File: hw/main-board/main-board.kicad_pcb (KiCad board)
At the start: 2 copper layers, 42 x 42 mm, 26 parts, among them J1 USB_C_Receptacle_USB2.0_16P, Q1 AONR21307, U1 HUSB238_xxxDD, U2 AP63205WU, U3 AP2112K-3.3, U4 PTR54L, U5 TMC2226-SA

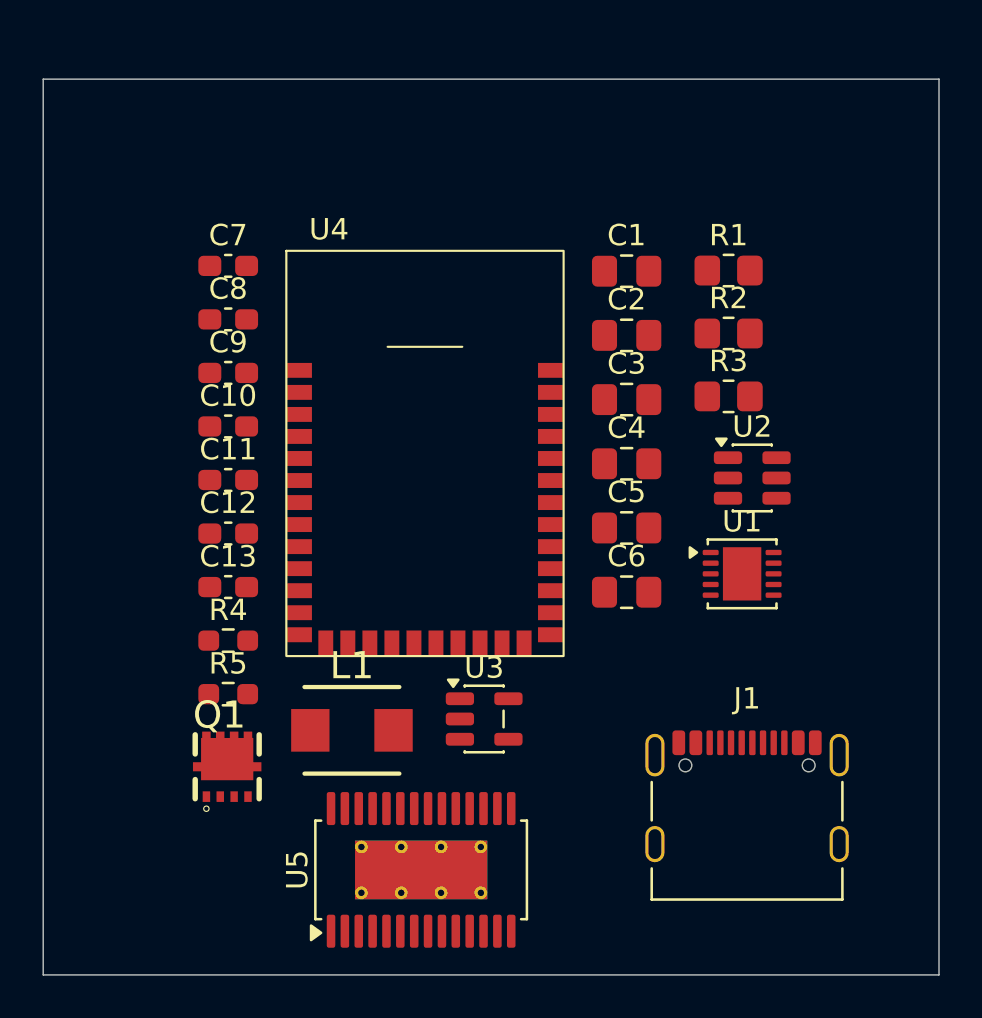
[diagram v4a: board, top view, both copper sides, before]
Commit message: Add TMC2226 circuit
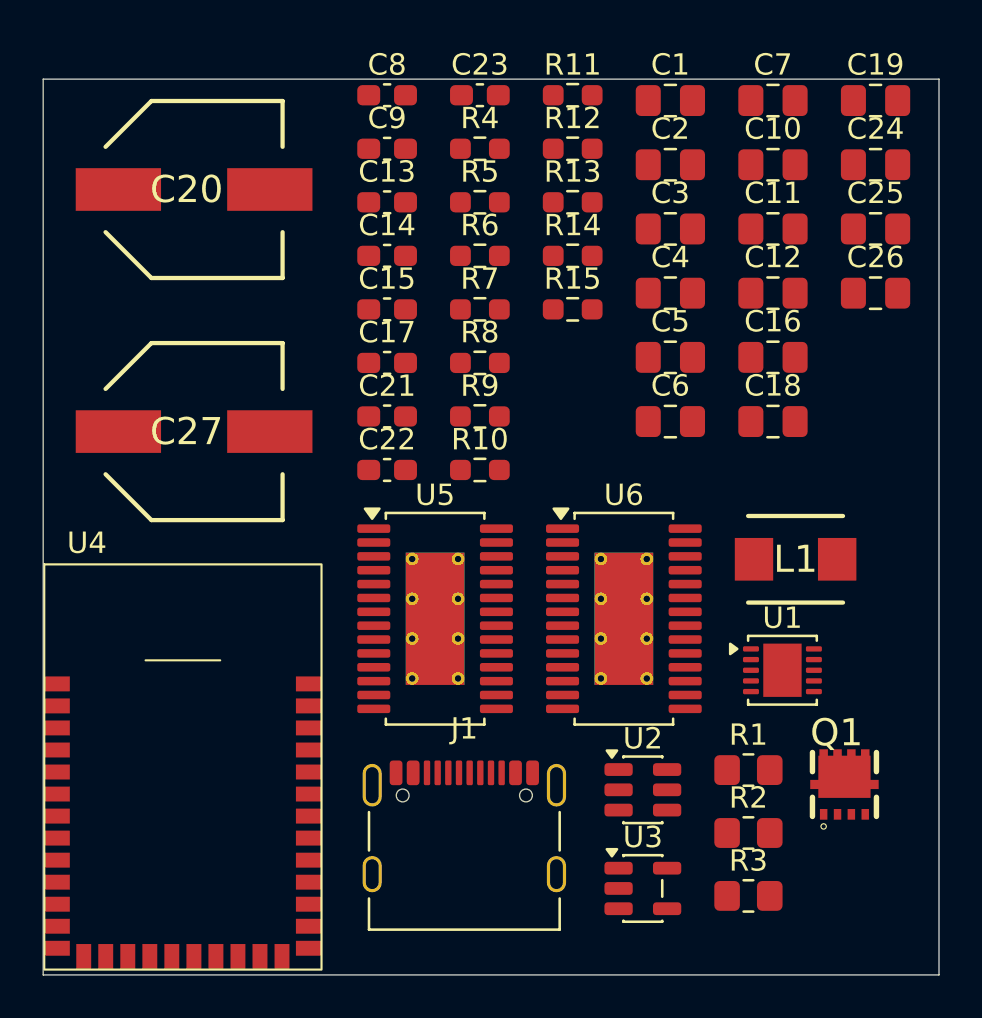
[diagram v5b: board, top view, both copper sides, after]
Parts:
- added C14: 22nF X7R 50V, Capacitor_SMD:C_0603_1608Metric_Pad1.08x0.95mm_HandSolder, F.Cu at (140.6, 81.8)
- added C15: 0.1uF X7R 16V, Capacitor_SMD:C_0603_1608Metric_Pad1.08x0.95mm_HandSolder, F.Cu at (140.6, 84.3)
- added C16: 4.7uF, Capacitor_SMD:C_0805_2012Metric_Pad1.18x1.45mm_HandSolder, F.Cu at (158.7, 86.5)
- added C17: 0.1uF X7R 16V, Capacitor_SMD:C_0603_1608Metric_Pad1.08x0.95mm_HandSolder, F.Cu at (140.6, 86.8)
- added C18: 0.1uF, Capacitor_SMD:C_0805_2012Metric_Pad1.18x1.45mm_HandSolder, F.Cu at (158.7, 89.6)
- added C19: 0.1uF, Capacitor_SMD:C_0805_2012Metric_Pad1.18x1.45mm_HandSolder, F.Cu at (163.5, 74.5)
- added C20: EEE-FK1V101P, Samacsys:EEHZT1E331UP, F.Cu at (131.6, 78.7)
- added C21: 0.1uF X7R 16V, Capacitor_SMD:C_0603_1608Metric_Pad1.08x0.95mm_HandSolder, F.Cu at (140.6, 89.3)
- added C22: 0.1uF X7R 16V, Capacitor_SMD:C_0603_1608Metric_Pad1.08x0.95mm_HandSolder, F.Cu at (140.6, 91.8)
- added C23: 22nF X7R 50V, Capacitor_SMD:C_0603_1608Metric_Pad1.08x0.95mm_HandSolder, F.Cu at (145.0, 74.3)
- added C24: 4.7uF, Capacitor_SMD:C_0805_2012Metric_Pad1.18x1.45mm_HandSolder, F.Cu at (163.5, 77.5)
- added C25: 0.1uF, Capacitor_SMD:C_0805_2012Metric_Pad1.18x1.45mm_HandSolder, F.Cu at (163.5, 80.5)
- added C26: 0.1uF, Capacitor_SMD:C_0805_2012Metric_Pad1.18x1.45mm_HandSolder, F.Cu at (163.5, 83.5)
- added C27: EEE-FK1V101P, Samacsys:EEHZT1E331UP, F.Cu at (131.6, 90.0)
- added R10: 8K2, Resistor_SMD:R_0603_1608Metric_Pad0.98x0.95mm_HandSolder, F.Cu at (145.0, 91.8)
- added R11: 1K, Resistor_SMD:R_0603_1608Metric_Pad0.98x0.95mm_HandSolder, F.Cu at (149.3, 74.3)
- added R12: 10K, Resistor_SMD:R_0603_1608Metric_Pad0.98x0.95mm_HandSolder, F.Cu at (149.3, 76.8)
- added R13: 10K, Resistor_SMD:R_0603_1608Metric_Pad0.98x0.95mm_HandSolder, F.Cu at (149.3, 79.3)
- added R14: 10K, Resistor_SMD:R_0603_1608Metric_Pad0.98x0.95mm_HandSolder, F.Cu at (149.3, 81.8)
- added R15: 8K2, Resistor_SMD:R_0603_1608Metric_Pad0.98x0.95mm_HandSolder, F.Cu at (149.3, 84.3)
- added R6: 10K, Resistor_SMD:R_0603_1608Metric_Pad0.98x0.95mm_HandSolder, F.Cu at (145.0, 81.8)
- added R7: 10K, Resistor_SMD:R_0603_1608Metric_Pad0.98x0.95mm_HandSolder, F.Cu at (145.0, 84.3)
- added R8: 1K, Resistor_SMD:R_0603_1608Metric_Pad0.98x0.95mm_HandSolder, F.Cu at (145.0, 86.8)
- added R9: 10K, Resistor_SMD:R_0603_1608Metric_Pad0.98x0.95mm_HandSolder, F.Cu at (145.0, 89.3)
- added U6: TMC2226-SA, Package_SO:HTSSOP-28-1EP_4.4x9.7mm_P0.65mm_EP2.75x6.2mm_ThermalVias, F.Cu at (151.7, 98.8)
- C10, C11, C12, C7: footprint Capacitor_SMD:C_0603_1608Metric_Pad1.08x0.95mm_HandSolder -> Capacitor_SMD:C_0805_2012Metric_Pad1.18x1.45mm_HandSolder
- moved Q1 29.0 mm to (162.1, 106.6)
- moved C10 28.3 mm to (158.7, 77.5)
- moved C11 28.1 mm to (158.7, 80.5)
- moved C12 27.9 mm to (158.7, 83.5)
- moved C7 26.7 mm to (158.7, 74.5)
- moved R4 25.9 mm to (145.0, 76.8)
- moved R5 25.9 mm to (145.0, 79.3)
- moved R1 23.4 mm to (157.6, 105.9)
- moved R2 23.4 mm to (157.6, 108.8)
- moved R3 23.4 mm to (157.6, 111.8)
- moved L1 22.3 mm to (159.8, 96.0)
- moved C13 19.5 mm to (140.6, 79.3)
- moved U4 18.6 mm to (131.1, 105.8)
- moved U2 15.5 mm to (152.6, 106.8)
- moved J1 13.3 mm to (144.2, 108.5)
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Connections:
- U5 pad 11: unconnected-(U5-5VOUT-Pad11) -> /VREF
- U5 pad 12: unconnected-(U5-MS1_AD0-Pad12) -> Net-(U5-MS1_AD0)
- U5 pad 14: unconnected-(U5-MS2_AD1-Pad14) -> Net-(U5-MS2_AD1)
- U5 pad 15: unconnected-(U5-DIAG-Pad15) -> /DIAG1
- U5 pad 17: unconnected-(U5-CLK-Pad17) -> GND
- U5 pad 18: unconnected-(U5-PDN_UART-Pad18) -> /UART_RX
- U5 pad 19: unconnected-(U5-VCC_IO-Pad19) -> +3.3V
- U5 pad 2: unconnected-(U5-BRB-Pad2) -> GND
- U5 pad 20: unconnected-(U5-STEP-Pad20) -> /STEP1
- U5 pad 21: unconnected-(U5-VREF-Pad21) -> Net-(U5-VREF)
- U5 pad 22: Net-(U5-GND-Pad22) -> GND
- U5 pad 23: unconnected-(U5-DIR-Pad23) -> /DIR1
- U5 pad 26: unconnected-(U5-VS-Pad26) -> VBUS
- U5 pad 27: unconnected-(U5-BRA-Pad27) -> GND
- U5 pad 29: Net-(U5-GND-Pad22) -> GND
- U5 pad 3: unconnected-(U5-VS-Pad3) -> VBUS
- U5 pad 5: unconnected-(U5-~{EN}-Pad5) -> /EN1
- U5 pad 6: Net-(U5-GND-Pad22) -> GND
- U5 pad 7: unconnected-(U5-CPO-Pad7) -> Net-(U5-CPO)
- U5 pad 8: unconnected-(U5-CPI-Pad8) -> Net-(U5-CPI)
- U5 pad 9: unconnected-(U5-VCP-Pad9) -> Net-(U5-VCP)

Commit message: Add connector for motor anf filtering caps for motor coils
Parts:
- added C28: 470pF X7R 100V, Capacitor_SMD:C_0805_2012Metric_Pad1.18x1.45mm_HandSolder, F.Cu at (163.5, 86.5)
- added C29: 470pF X7R 100V, Capacitor_SMD:C_0805_2012Metric_Pad1.18x1.45mm_HandSolder, F.Cu at (163.5, 89.6)
- added C30: 470pF X7R 100V, Capacitor_SMD:C_0805_2012Metric_Pad1.18x1.45mm_HandSolder, F.Cu at (168.3, 74.5)
- added C31: 470pF X7R 100V, Capacitor_SMD:C_0805_2012Metric_Pad1.18x1.45mm_HandSolder, F.Cu at (168.3, 77.5)
- added C32: 470pF X7R 100V, Capacitor_SMD:C_0805_2012Metric_Pad1.18x1.45mm_HandSolder, F.Cu at (168.3, 80.5)
- added C33: 470pF X7R 100V, Capacitor_SMD:C_0805_2012Metric_Pad1.18x1.45mm_HandSolder, F.Cu at (168.3, 83.5)
- added C34: 470pF X7R 100V, Capacitor_SMD:C_0805_2012Metric_Pad1.18x1.45mm_HandSolder, F.Cu at (168.3, 86.5)
- added C35: 470pF X7R 100V, Capacitor_SMD:C_0805_2012Metric_Pad1.18x1.45mm_HandSolder, F.Cu at (168.3, 89.6)
- added J2: 22-23-2041, Samacsys:SHDR4W87P0X254_1X4_1001X635X1105P, F.Cu at (140.4, 97.0)
- added J3: 22-23-2041, Samacsys:SHDR4W87P0X254_1X4_1001X635X1105P, F.Cu at (140.4, 104.9)
- moved L1 21.3 mm to (165.2, 116.6)
- moved U1 19.6 mm to (146.2, 115.9)
- moved Q1 17.3 mm to (145.3, 111.0)
- moved R1 17.3 mm to (140.8, 110.4)
- moved R2 17.3 mm to (140.8, 113.3)
- moved R3 17.3 mm to (140.8, 116.3)
- moved J1 11.6 mm to (155.8, 108.5)
- moved U2 11.6 mm to (164.2, 106.8)
- moved U3 11.6 mm to (164.2, 111.4)
- moved U5 11.6 mm to (154.4, 98.8)
- moved U6 11.6 mm to (163.3, 98.8)
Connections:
- U5 pad 1: unconnected-(U5-OB1-Pad1) -> Net-(U5-OB1)
- U5 pad 25: unconnected-(U5-OA2-Pad25) -> Net-(U5-OA2)
- U5 pad 28: unconnected-(U5-OA1-Pad28) -> Net-(U5-OA1)
- U5 pad 4: unconnected-(U5-OB2-Pad4) -> Net-(U5-OB2)
- U6 pad 1: unconnected-(U6-OB1-Pad1) -> Net-(U6-OB1)
- U6 pad 25: unconnected-(U6-OA2-Pad25) -> Net-(U6-OA2)
- U6 pad 28: unconnected-(U6-OA1-Pad28) -> Net-(U6-OA1)
- U6 pad 4: unconnected-(U6-OB2-Pad4) -> Net-(U6-OB2)

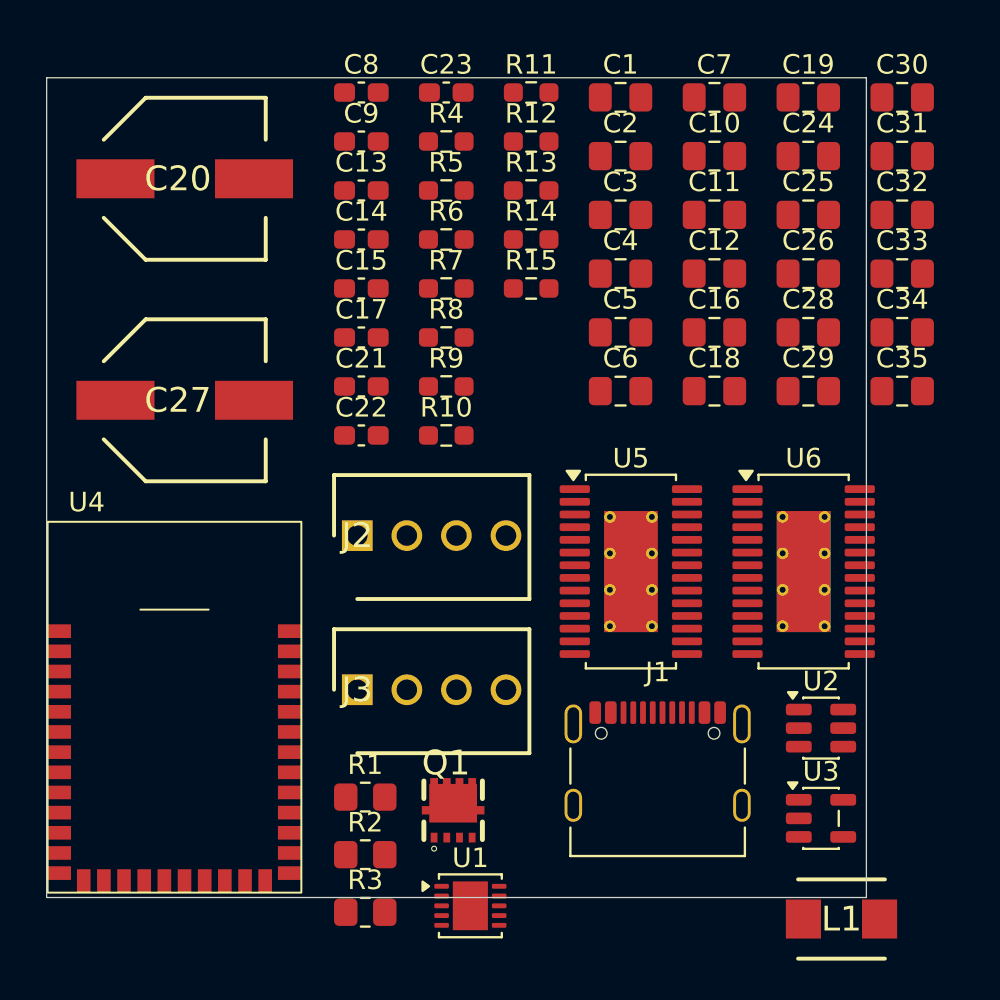
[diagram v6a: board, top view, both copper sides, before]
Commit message: Connector for motor changed, filtering cap changed
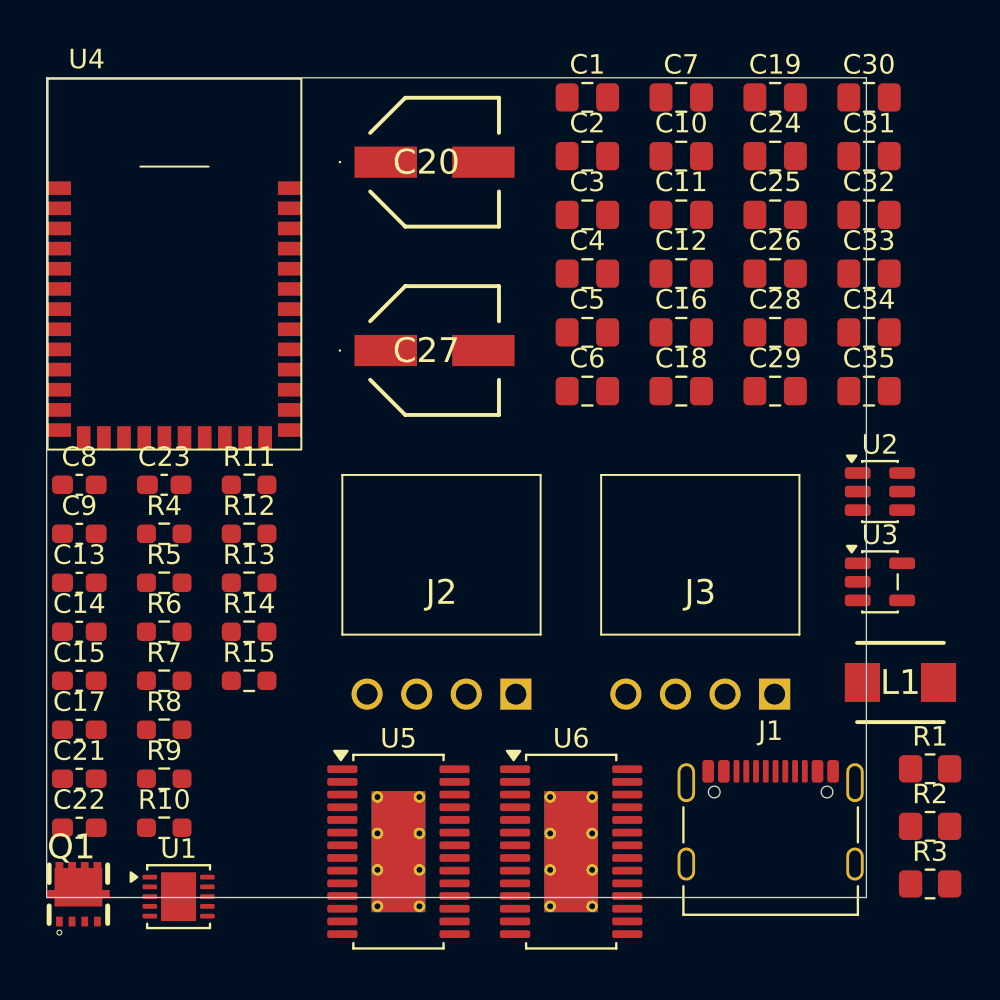
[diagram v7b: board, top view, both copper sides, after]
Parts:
- C20, C27: value EEE-FK1V101P -> EEE-FT1V101AP; footprint Samacsys:EEHZT1E331UP -> Samacsys:EEE1AA101SP
- J2, J3: value 22-23-2041 -> 22-05-3041; footprint Samacsys:SHDR4W87P0X254_1X4_1001X635X1105P -> Samacsys:22053041
- moved R1 29.0 mm to (169.8, 108.9)
- moved R2 29.0 mm to (169.8, 111.9)
- moved R3 29.0 mm to (169.8, 114.8)
- moved C14 24.8 mm to (126.2, 101.9)
- moved C21 24.8 mm to (126.2, 109.4)
- moved C8 24.8 mm to (126.2, 94.4)
- moved C13 24.8 mm to (126.2, 99.4)
- moved C15 24.8 mm to (126.2, 104.4)
- moved C17 24.8 mm to (126.2, 106.9)
- moved C22 24.8 mm to (126.2, 111.9)
- moved C23 24.8 mm to (130.5, 94.4)
- moved C9 24.8 mm to (126.2, 96.9)
- moved R11 24.8 mm to (134.9, 94.4)
- moved R14 24.8 mm to (134.9, 101.9)
- moved R6 24.8 mm to (130.5, 101.9)
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
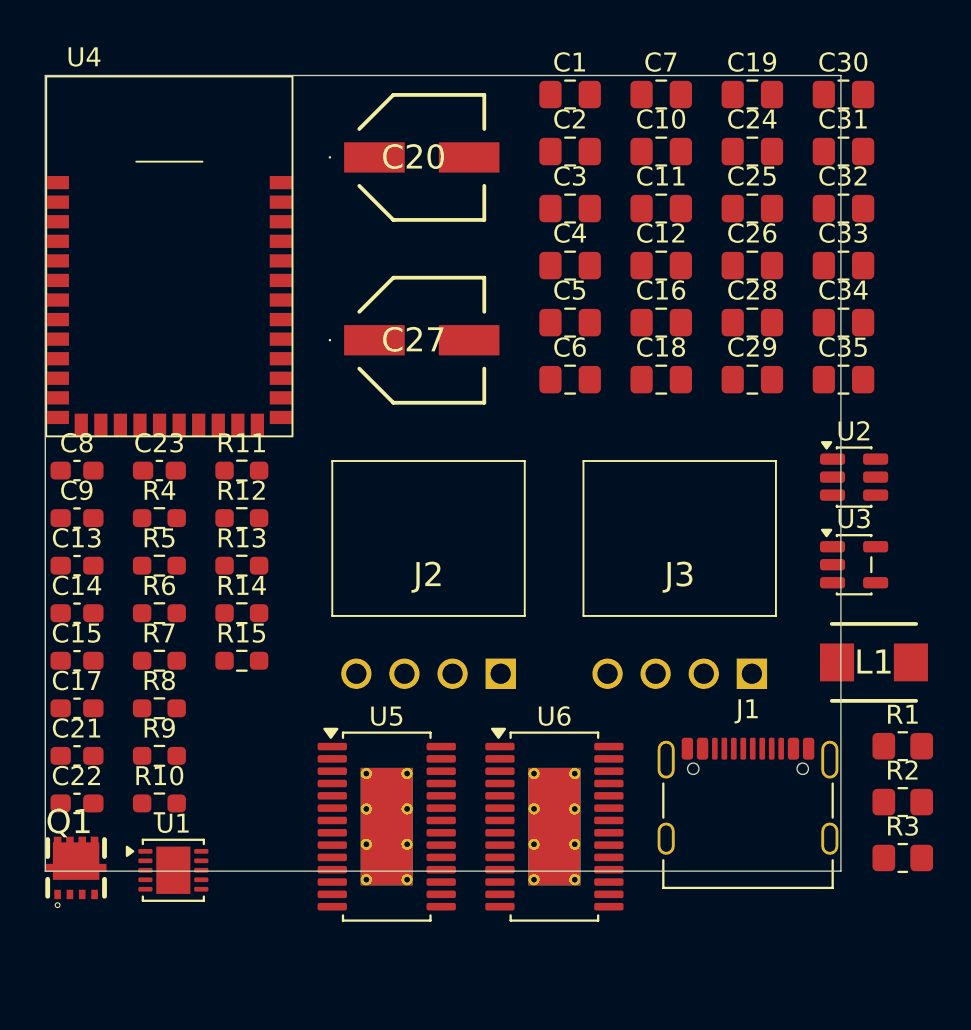
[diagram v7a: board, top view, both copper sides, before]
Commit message: Change connector for motor to smaller one
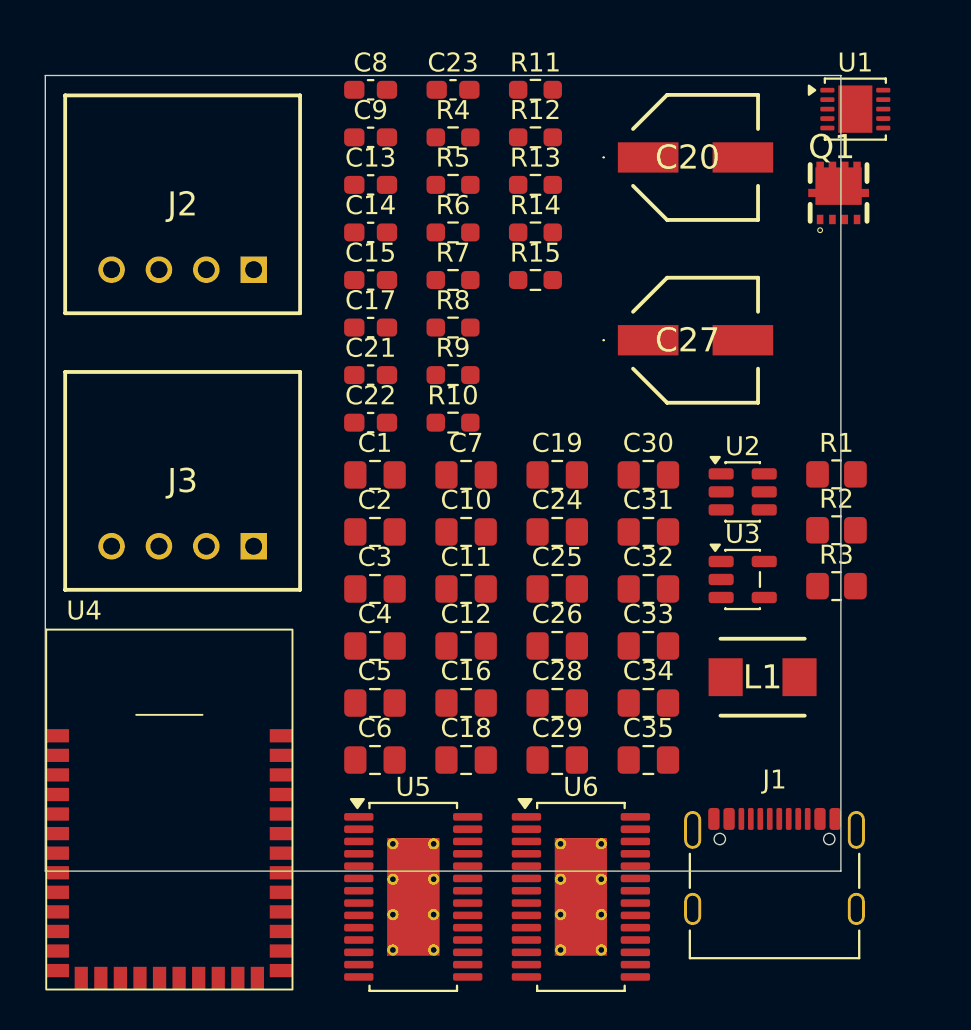
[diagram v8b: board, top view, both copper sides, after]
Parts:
- J2, J3: value 22-05-3041 -> S4B-XH-A_LF__SN_; footprint Samacsys:22053041 -> Samacsys:S4BXHALFSN
- moved U1 53.9 mm to (167.3, 75.3)
- moved Q1 53.8 mm to (166.4, 79.7)
- moved U4 29.2 mm to (131.1, 112.2)
- moved J3 27.1 mm to (135.5, 98.3)
- moved C14 25.4 mm to (141.7, 81.8)
- moved C21 25.4 mm to (141.7, 89.3)
- moved C8 25.4 mm to (141.7, 74.3)
- moved C23 25.4 mm to (146.0, 74.3)
- moved R11 25.4 mm to (150.4, 74.3)
- moved R14 25.4 mm to (150.4, 81.8)
- moved R6 25.4 mm to (146.0, 81.8)
- moved R9 25.4 mm to (146.0, 89.3)
- moved C13 25.4 mm to (141.7, 79.3)
- moved C15 25.4 mm to (141.7, 84.3)
- moved C17 25.4 mm to (141.7, 86.8)
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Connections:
- J2 pad 1: Net-(U5-OA1) -> Net-(U5-OB2)
- J2 pad 2: Net-(U5-OA2) -> Net-(U5-OB1)
- J2 pad 3: Net-(U5-OB1) -> Net-(U5-OA2)
- J2 pad 4: Net-(U5-OB2) -> Net-(U5-OA1)
- J3 pad 1: Net-(U6-OA1) -> Net-(U6-OB2)
- J3 pad 2: Net-(U6-OA2) -> Net-(U6-OB1)
- J3 pad 3: Net-(U6-OB1) -> Net-(U6-OA2)
- J3 pad 4: Net-(U6-OB2) -> Net-(U6-OA1)
